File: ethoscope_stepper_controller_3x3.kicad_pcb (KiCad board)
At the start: 2 copper layers, 74.9 x 74.9 mm, 69 parts, among them P1 PWR_JACK_2.1x5.5_SMD_VERT, T1 TERM_BLK, T2 TERM_BLK, T3 TERM_BLK, T4 TERM_BLK, T5 TERM_BLK, T6 TERM_BLK, T7 TERM_BLK, U1 TMC429, U10 DRV8846, U11 TMC429, U12 BUFFER_TRI_STATE, U13 DRV8846, U2 BUFFER_TRI_STATE, U3 DRV8846, U4 DRV8846, U5 DRV8846, U6 TMC429, U7 BUFFER_TRI_STATE, U8 DRV8846, U9 DRV8846

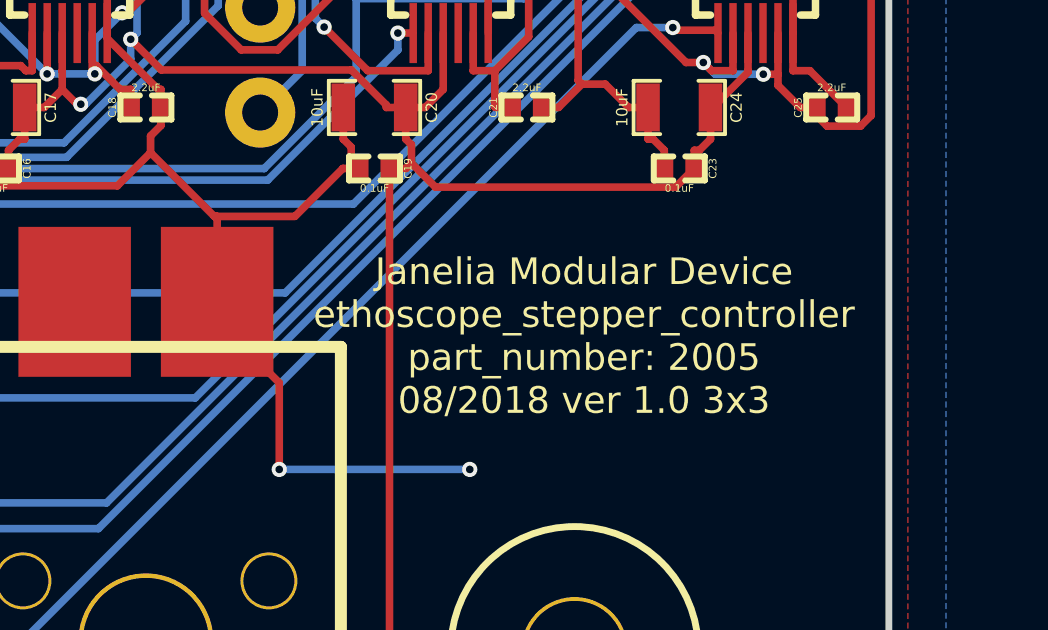
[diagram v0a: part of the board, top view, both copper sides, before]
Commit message: ethoscope_stepper_controller -> ethoscope_stepper_controller_3x3.
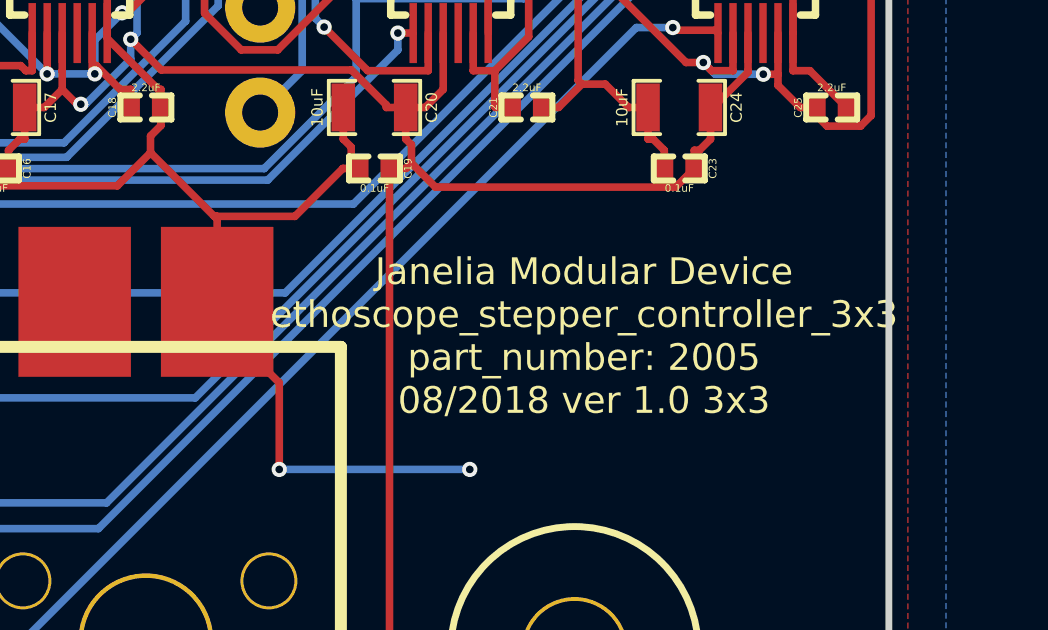
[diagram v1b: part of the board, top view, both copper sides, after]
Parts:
- C1, C11, C12, C13, C15, C16, C18, C19, C2, C21, C22, C23, C25, C3, C5, C6, C8, C9, R1, R10, R11, R12, R13, R14, R15, R16, R17, R2, R3, R4, R5, R6, R7, R8, R9: footprint ethoscope_stepper_controller:SM0402 -> ethoscope_stepper_controller_3x3:SM0402
- C10, C14, C17, C20, C24, C4, C7: footprint ethoscope_stepper_controller:SM0805 -> ethoscope_stepper_controller_3x3:SM0805
- CLK1: footprint ethoscope_stepper_controller:CTS_SMD_4_7X5MM -> ethoscope_stepper_controller_3x3:CTS_SMD_4_7X5MM
- MH1, MH2, MH3, MH4: footprint ethoscope_stepper_controller:MOUNTING_HOLE_4-40 -> ethoscope_stepper_controller_3x3:MOUNTING_HOLE_4-40
- P1: footprint ethoscope_stepper_controller:DCJACK_3PIN_SMD_VERT -> ethoscope_stepper_controller_3x3:DCJACK_3PIN_SMD_VERT
- T1, T2, T3, T4, T5, T6, T7: footprint ethoscope_stepper_controller:TERM_BLK_HDR_4POS_VERT_0.138IN -> ethoscope_stepper_controller_3x3:TERM_BLK_HDR_4POS_VERT_0.138IN
- TEENSY1: footprint ethoscope_stepper_controller:TEENSY_3.5_MIN -> ethoscope_stepper_controller_3x3:TEENSY_3.5_MIN
- U1, U11, U6: footprint ethoscope_stepper_controller:QFN-5x5-32 -> ethoscope_stepper_controller_3x3:QFN-5x5-32
- U10, U13, U3, U4, U5, U8, U9: footprint ethoscope_stepper_controller:VQFN-4x4-24 -> ethoscope_stepper_controller_3x3:VQFN-4x4-24
- U12, U2, U7: footprint ethoscope_stepper_controller:SOT-23-5 -> ethoscope_stepper_controller_3x3:SOT-23-5
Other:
- board text added: "Janelia Modular Device ethoscope_stepper_controller_3x3 part_number: 2005 08/2018 ver 1.0 3x3"
- board text removed: "Janelia Modular Device ethoscope_stepper_controller part_number: 2005 08/2018 ver 1.0 3x3"

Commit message: Finished version 1.0.
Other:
- board text added: "Janelia Modular Device ethoscope_stepper_controller part_number: 2005 08/2018 ver 1.0 3x3"
- board text removed: "Janelia Modular Device ethoscope_stepper_controller_3x3 part_number: 2005 08/2018 ver 1.0 3x3"
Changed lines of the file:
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@@
     (effects (font (size 1.016 1.016) (thickness 0.1905)))
   )
-  (gr_text "Janelia Modular Device\nethoscope_stepper_controller_3x3\npart_number: 2005\n08/2018 ver 1.0 3x3" (at 179.705 118.11) (layer F.SilkS)
+  (gr_text "Janelia Modular Device\nethoscope_stepper_controller\npart_number: 2005\n08/2018 ver 1.0 3x3" (at 179.705 118.11) (layer F.SilkS)
     (effects (font (size 0.889 0.889) (thickness 0.22225)))
   )

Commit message: Rearranged schematics.
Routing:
- net GND: track 490.5 -> 0.00 mm, vias 12 -> 0
- net VAA: track 145.8 -> 0.00 mm, vias 6 -> 0
- net +3V3: track 145.4 -> 0.00 mm, vias 4 -> 0
- net /ENABLE_ALL: track 140.4 -> 0.00 mm, vias 7 -> 0
- net /CS_429_2: track 81.4 -> 0.00 mm
- net /tmc429_0/DIR_1: track 73.2 -> 0.00 mm
- net /tmc429_2/DIR_0: track 70.9 -> 0.00 mm, vias 2 -> 0
- net /tmc429_1/STEP_0: track 67.9 -> 0.00 mm, vias 2 -> 0
- net /tmc429_2/STEP_0: track 66.7 -> 0.00 mm, vias 2 -> 0
- net /MOSI: track 64.5 -> 0.00 mm, vias 3 -> 0
- net /CS_429_1: track 64.2 -> 0.00 mm, vias 1 -> 0
- net /tmc429_0/STEP_1: track 64.0 -> 0.00 mm, vias 2 -> 0
- net /tmc429_1/DIR_0: track 63.9 -> 0.00 mm, vias 2 -> 0
- net /tmc429_1/STEP_2: track 59.1 -> 0.00 mm
- net /tmc429_1/DIR_2: track 54.2 -> 0.00 mm, vias 2 -> 0
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- removed copper zone on B.Cu, net GND
- removed copper zone on F.Cu, net GND
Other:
- outline, holes or cut-outs redrawn
- board text added: "Janelia Modular Device ethoscope_stepper_controller part_number: 2005 09/2018 ver 1.1 3x3"
- board text removed: "Janelia Modular Device ethoscope_stepper_controller part_number: 2005 08/2018 ver 1.0 3x3"

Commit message: Ready for autorouting.
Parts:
- T1, T2, T3, T4, T5, T6, T7: value TERM_BLK -> TERM_BLK_HDR_4POS_VERT_0.138IN
- TEENSY1: value TEENSY_3.5 -> TEENSY_3.5_MIN
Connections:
- net /CLK renamed /ethoscope_3x3/CLK
- net /CS_429_0 renamed /~CS_429_0
- net /CS_429_1 renamed /~CS_429_1
- net /CS_429_2 renamed /~CS_429_2
- net /tmc429_0/DIR_0 renamed /ethoscope_3x3/tmc429_0/DIR_0
- net /tmc429_0/DIR_1 renamed /ethoscope_3x3/tmc429_0/DIR_1
- net /tmc429_0/DIR_2 renamed /ethoscope_3x3/tmc429_0/DIR_2
- net /tmc429_0/MISO_UB renamed /ethoscope_3x3/tmc429_0/MISO_UB
- net /tmc429_0/STEP_0 renamed /ethoscope_3x3/tmc429_0/STEP_0
- net /tmc429_0/STEP_1 renamed /ethoscope_3x3/tmc429_0/STEP_1
- net /tmc429_0/STEP_2 renamed /ethoscope_3x3/tmc429_0/STEP_2
- net /tmc429_0/stepper_driver_0/AISEN renamed /ethoscope_3x3/tmc429_0/stepper_driver_0/AISEN
- net /tmc429_0/stepper_driver_0/A_+ renamed /ethoscope_3x3/tmc429_0/stepper_driver_0/A_+
- net /tmc429_0/stepper_driver_0/A_- renamed /ethoscope_3x3/tmc429_0/stepper_driver_0/A_-
- net /tmc429_0/stepper_driver_0/BISEN renamed /ethoscope_3x3/tmc429_0/stepper_driver_0/BISEN
- net /tmc429_0/stepper_driver_0/B_+ renamed /ethoscope_3x3/tmc429_0/stepper_driver_0/B_+
- net /tmc429_0/stepper_driver_0/B_- renamed /ethoscope_3x3/tmc429_0/stepper_driver_0/B_-
- net /tmc429_0/stepper_driver_1/AISEN renamed /ethoscope_3x3/tmc429_0/stepper_driver_1/AISEN
- net /tmc429_0/stepper_driver_1/A_+ renamed /ethoscope_3x3/tmc429_0/stepper_driver_1/A_+
- net /tmc429_0/stepper_driver_1/A_- renamed /ethoscope_3x3/tmc429_0/stepper_driver_1/A_-
- net /tmc429_0/stepper_driver_1/BISEN renamed /ethoscope_3x3/tmc429_0/stepper_driver_1/BISEN
- net /tmc429_0/stepper_driver_1/B_+ renamed /ethoscope_3x3/tmc429_0/stepper_driver_1/B_+
- net /tmc429_0/stepper_driver_1/B_- renamed /ethoscope_3x3/tmc429_0/stepper_driver_1/B_-
- net /tmc429_0/stepper_driver_2/AISEN renamed /ethoscope_3x3/tmc429_0/stepper_driver_2/AISEN
- net /tmc429_0/stepper_driver_2/A_+ renamed /ethoscope_3x3/tmc429_0/stepper_driver_2/A_+
- net /tmc429_0/stepper_driver_2/A_- renamed /ethoscope_3x3/tmc429_0/stepper_driver_2/A_-
- net /tmc429_0/stepper_driver_2/BISEN renamed /ethoscope_3x3/tmc429_0/stepper_driver_2/BISEN
- net /tmc429_0/stepper_driver_2/B_+ renamed /ethoscope_3x3/tmc429_0/stepper_driver_2/B_+
- net /tmc429_0/stepper_driver_2/B_- renamed /ethoscope_3x3/tmc429_0/stepper_driver_2/B_-
- net /tmc429_1/DIR_0 renamed /ethoscope_3x3/tmc429_1/DIR_0
- net /tmc429_1/DIR_1 renamed /ethoscope_3x3/tmc429_1/DIR_1
- net /tmc429_1/DIR_2 renamed /ethoscope_3x3/tmc429_1/DIR_2
- net /tmc429_1/MISO_UB renamed /ethoscope_3x3/tmc429_1/MISO_UB
- net /tmc429_1/STEP_0 renamed /ethoscope_3x3/tmc429_1/STEP_0
- net /tmc429_1/STEP_1 renamed /ethoscope_3x3/tmc429_1/STEP_1
- net /tmc429_1/STEP_2 renamed /ethoscope_3x3/tmc429_1/STEP_2
- net /tmc429_1/stepper_driver_0/AISEN renamed /ethoscope_3x3/tmc429_1/stepper_driver_0/AISEN
- net /tmc429_1/stepper_driver_0/A_+ renamed /ethoscope_3x3/tmc429_1/stepper_driver_0/A_+
- net /tmc429_1/stepper_driver_0/A_- renamed /ethoscope_3x3/tmc429_1/stepper_driver_0/A_-
- net /tmc429_1/stepper_driver_0/BISEN renamed /ethoscope_3x3/tmc429_1/stepper_driver_0/BISEN
- net /tmc429_1/stepper_driver_0/B_+ renamed /ethoscope_3x3/tmc429_1/stepper_driver_0/B_+
- net /tmc429_1/stepper_driver_0/B_- renamed /ethoscope_3x3/tmc429_1/stepper_driver_0/B_-
- net /tmc429_1/stepper_driver_1/AISEN renamed /ethoscope_3x3/tmc429_1/stepper_driver_1/AISEN
- net /tmc429_1/stepper_driver_1/A_+ renamed /ethoscope_3x3/tmc429_1/stepper_driver_1/A_+
- net /tmc429_1/stepper_driver_1/A_- renamed /ethoscope_3x3/tmc429_1/stepper_driver_1/A_-
- net /tmc429_1/stepper_driver_1/BISEN renamed /ethoscope_3x3/tmc429_1/stepper_driver_1/BISEN
- net /tmc429_1/stepper_driver_1/B_+ renamed /ethoscope_3x3/tmc429_1/stepper_driver_1/B_+
- net /tmc429_1/stepper_driver_1/B_- renamed /ethoscope_3x3/tmc429_1/stepper_driver_1/B_-
- net /tmc429_1/stepper_driver_2/AISEN renamed /ethoscope_3x3/tmc429_1/stepper_driver_2/AISEN
- net /tmc429_1/stepper_driver_2/A_+ renamed /ethoscope_3x3/tmc429_1/stepper_driver_2/A_+
- net /tmc429_1/stepper_driver_2/A_- renamed /ethoscope_3x3/tmc429_1/stepper_driver_2/A_-
- net /tmc429_1/stepper_driver_2/BISEN renamed /ethoscope_3x3/tmc429_1/stepper_driver_2/BISEN
- net /tmc429_1/stepper_driver_2/B_+ renamed /ethoscope_3x3/tmc429_1/stepper_driver_2/B_+
- net /tmc429_1/stepper_driver_2/B_- renamed /ethoscope_3x3/tmc429_1/stepper_driver_2/B_-
- net /tmc429_2/DIR_0 renamed /ethoscope_3x3/tmc_429_2/DIR_0
- net /tmc429_2/MISO_UB renamed /ethoscope_3x3/tmc_429_2/MISO_UB
- net /tmc429_2/STEP_0 renamed /ethoscope_3x3/tmc_429_2/STEP_0
- net /tmc429_2/stepper_driver_0/AISEN renamed /ethoscope_3x3/tmc_429_2/stepper_driver_0/AISEN
- net /tmc429_2/stepper_driver_0/A_+ renamed /ethoscope_3x3/tmc_429_2/stepper_driver_0/A_+
- net /tmc429_2/stepper_driver_0/A_- renamed /ethoscope_3x3/tmc_429_2/stepper_driver_0/A_-
- net /tmc429_2/stepper_driver_0/BISEN renamed /ethoscope_3x3/tmc_429_2/stepper_driver_0/BISEN
- net /tmc429_2/stepper_driver_0/B_+ renamed /ethoscope_3x3/tmc_429_2/stepper_driver_0/B_+
- net /tmc429_2/stepper_driver_0/B_- renamed /ethoscope_3x3/tmc_429_2/stepper_driver_0/B_-
- C11 pad 1: /tmc429_0/stepper_driver_2/VINT -> /ethoscope_3x3/tmc429_0/stepper_driver_2/VINT
- C15 pad 1: /tmc429_1/stepper_driver_0/VINT -> /ethoscope_3x3/tmc429_1/stepper_driver_0/VINT
- C18 pad 1: /tmc429_1/stepper_driver_1/VINT -> /ethoscope_3x3/tmc429_1/stepper_driver_1/VINT
- C21 pad 1: /tmc429_1/stepper_driver_2/VINT -> /ethoscope_3x3/tmc429_1/stepper_driver_2/VINT
- C25 pad 1: /tmc429_2/stepper_driver_0/VINT -> /ethoscope_3x3/tmc_429_2/stepper_driver_0/VINT
- C5 pad 1: /tmc429_0/stepper_driver_0/VINT -> /ethoscope_3x3/tmc429_0/stepper_driver_0/VINT
- C8 pad 1: /tmc429_0/stepper_driver_1/VINT -> /ethoscope_3x3/tmc429_0/stepper_driver_1/VINT
- TEENSY1 pad 22: /ENABLE_ALL -> /~SLEEP
- U10 pad 11: /ENABLE_ALL -> (no net)
- U10 pad 14: /tmc429_1/stepper_driver_2/VINT -> /ethoscope_3x3/tmc429_1/stepper_driver_2/VINT
- U10 pad 17: /tmc429_1/stepper_driver_2/VINT -> /ethoscope_3x3/tmc429_1/stepper_driver_2/VINT
- U10 pad 19: /tmc429_1/stepper_driver_2/VINT -> +3V3
- U10 pad 22: /tmc429_1/stepper_driver_2/VINT -> +3V3
- U10 pad 23: /tmc429_1/stepper_driver_2/VINT -> /~SLEEP
- U10 pad 24: /tmc429_1/stepper_driver_2/VINT -> +3V3
- U10 pad 9: /tmc429_1/stepper_driver_2/VINT -> +3V3
- U13 pad 11: /ENABLE_ALL -> (no net)
- U13 pad 14: /tmc429_2/stepper_driver_0/VINT -> /ethoscope_3x3/tmc_429_2/stepper_driver_0/VINT
- U13 pad 17: /tmc429_2/stepper_driver_0/VINT -> /ethoscope_3x3/tmc_429_2/stepper_driver_0/VINT
- U13 pad 19: /tmc429_2/stepper_driver_0/VINT -> +3V3
- U13 pad 22: /tmc429_2/stepper_driver_0/VINT -> +3V3
- U13 pad 23: /tmc429_2/stepper_driver_0/VINT -> /~SLEEP
- U13 pad 24: /tmc429_2/stepper_driver_0/VINT -> +3V3
- U13 pad 9: /tmc429_2/stepper_driver_0/VINT -> +3V3
- U3 pad 11: /ENABLE_ALL -> (no net)
- U3 pad 14: /tmc429_0/stepper_driver_0/VINT -> /ethoscope_3x3/tmc429_0/stepper_driver_0/VINT
- U3 pad 17: /tmc429_0/stepper_driver_0/VINT -> /ethoscope_3x3/tmc429_0/stepper_driver_0/VINT
- U3 pad 19: /tmc429_0/stepper_driver_0/VINT -> +3V3
- U3 pad 22: /tmc429_0/stepper_driver_0/VINT -> +3V3
- U3 pad 23: /tmc429_0/stepper_driver_0/VINT -> /~SLEEP
- U3 pad 24: /tmc429_0/stepper_driver_0/VINT -> +3V3
- U3 pad 9: /tmc429_0/stepper_driver_0/VINT -> +3V3
- U4 pad 11: /ENABLE_ALL -> (no net)
- U4 pad 14: /tmc429_0/stepper_driver_1/VINT -> /ethoscope_3x3/tmc429_0/stepper_driver_1/VINT
- U4 pad 17: /tmc429_0/stepper_driver_1/VINT -> /ethoscope_3x3/tmc429_0/stepper_driver_1/VINT
- U4 pad 19: /tmc429_0/stepper_driver_1/VINT -> +3V3
- U4 pad 22: /tmc429_0/stepper_driver_1/VINT -> +3V3
- U4 pad 23: /tmc429_0/stepper_driver_1/VINT -> /~SLEEP
- U4 pad 24: /tmc429_0/stepper_driver_1/VINT -> +3V3
- U4 pad 9: /tmc429_0/stepper_driver_1/VINT -> +3V3
- U5 pad 11: /ENABLE_ALL -> (no net)
- U5 pad 14: /tmc429_0/stepper_driver_2/VINT -> /ethoscope_3x3/tmc429_0/stepper_driver_2/VINT
- U5 pad 17: /tmc429_0/stepper_driver_2/VINT -> /ethoscope_3x3/tmc429_0/stepper_driver_2/VINT
- U5 pad 19: /tmc429_0/stepper_driver_2/VINT -> +3V3
- U5 pad 22: /tmc429_0/stepper_driver_2/VINT -> +3V3
- U5 pad 23: /tmc429_0/stepper_driver_2/VINT -> /~SLEEP
- U5 pad 24: /tmc429_0/stepper_driver_2/VINT -> +3V3
- U5 pad 9: /tmc429_0/stepper_driver_2/VINT -> +3V3
- U8 pad 11: /ENABLE_ALL -> (no net)
- U8 pad 14: /tmc429_1/stepper_driver_0/VINT -> /ethoscope_3x3/tmc429_1/stepper_driver_0/VINT
- U8 pad 17: /tmc429_1/stepper_driver_0/VINT -> /ethoscope_3x3/tmc429_1/stepper_driver_0/VINT
- U8 pad 19: /tmc429_1/stepper_driver_0/VINT -> +3V3
- U8 pad 22: /tmc429_1/stepper_driver_0/VINT -> +3V3
- U8 pad 23: /tmc429_1/stepper_driver_0/VINT -> /~SLEEP
- U8 pad 24: /tmc429_1/stepper_driver_0/VINT -> +3V3
- U8 pad 9: /tmc429_1/stepper_driver_0/VINT -> +3V3
- U9 pad 11: /ENABLE_ALL -> (no net)
- U9 pad 14: /tmc429_1/stepper_driver_1/VINT -> /ethoscope_3x3/tmc429_1/stepper_driver_1/VINT
- U9 pad 17: /tmc429_1/stepper_driver_1/VINT -> /ethoscope_3x3/tmc429_1/stepper_driver_1/VINT
- U9 pad 19: /tmc429_1/stepper_driver_1/VINT -> +3V3
- U9 pad 22: /tmc429_1/stepper_driver_1/VINT -> +3V3
- U9 pad 23: /tmc429_1/stepper_driver_1/VINT -> /~SLEEP
- U9 pad 24: /tmc429_1/stepper_driver_1/VINT -> +3V3
- U9 pad 9: /tmc429_1/stepper_driver_1/VINT -> +3V3
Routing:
- net GND: track 0.00 -> 6.50 mm
- net +3V3: track 0.00 -> 5.70 mm
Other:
- net class SIGNAL: trace_width 0.254 -> 0.2032

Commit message: Finished autorouting.
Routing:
- net GND: track 6.50 -> 441.3 mm, vias 0 -> 4
- net +3V3: track 5.70 -> 415.5 mm, vias 0 -> 15
- net /~SLEEP: track 0.00 -> 150.4 mm, vias 0 -> 7
- net VAA: track 0.00 -> 140.2 mm, vias 0 -> 8
- net /ethoscope_3x3/tmc_429_2/STEP_0: track 0.00 -> 74.3 mm, vias 0 -> 2
- net /MOSI: track 0.00 -> 73.8 mm, vias 0 -> 3
- net /~CS_429_2: track 0.00 -> 69.1 mm, vias 0 -> 3
- net /ethoscope_3x3/tmc429_0/DIR_1: track 0.00 -> 68.7 mm, vias 0 -> 2
- net /ethoscope_3x3/tmc_429_2/DIR_0: track 0.00 -> 67.1 mm, vias 0 -> 2
- net /ethoscope_3x3/tmc429_0/STEP_1: track 0.00 -> 64.3 mm, vias 0 -> 2
- net /~CS_429_1: track 0.00 -> 63.9 mm, vias 0 -> 1
- net /ethoscope_3x3/tmc429_1/STEP_2: track 0.00 -> 61.9 mm
- net /ethoscope_3x3/tmc429_1/STEP_0: track 0.00 -> 61.9 mm, vias 0 -> 2
- net /ethoscope_3x3/tmc429_1/DIR_2: track 0.00 -> 58.5 mm, vias 0 -> 2
- net /ethoscope_3x3/tmc429_1/DIR_0: track 0.00 -> 57.7 mm, vias 0 -> 2
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
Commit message: Finished version 1.0.
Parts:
- added L1: LED_24V_RED, ethoscope_stepper_controller_3x3:LED_555-3XXX_R, F.Cu at (153.7, 134.0)
- added L2: LED_5V_GRN, ethoscope_stepper_controller_3x3:LED_555-3XXX_G, F.Cu at (151.1, 134.0)
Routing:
- net +3V3: track 415.5 -> 460.5 mm
- net GND: track 441.3 -> 455.9 mm
- net VAA: track 140.2 -> 152.0 mm
- net /ethoscope_3x3/tmc_429_2/stepper_driver_0/A_+: track 39.6 -> 40.2 mm
- added copper zone on B.Cu, net GND
- added copper zone on F.Cu, net VAA
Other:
- rule solder_mask_min_width: 0.25 -> 0.1016
- board text added: "0"
- board text added: "1"
- board text added: "2"
- board text added: "3"
- board text added: "4"
- board text added: "5"
- board text added: "6"
- board text added: "POWER"
- board text added: "USB"

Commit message: Progress towards v1.2
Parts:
- R10, R11, R12, R13, R14, R16, R17, R2, R3, R4, R5, R6, R7, R9: value 5.1 -> 2.2; footprint ethoscope_stepper_controller_3x3:SM0402 -> footprints:SM0402
- TEENSY1: value TEENSY_3.5_MIN -> TEENSY_3.5
- moved C17 4.49 mm to (164.5, 111.1), turned to 0 degrees
- moved C20 4.49 mm to (177.2, 111.1), turned to 0 degrees
- moved C24 4.49 mm to (187.3, 111.1), turned to 0 degrees
- moved C4 4.49 mm to (164.5, 78.1), turned to 0 degrees
- moved C10 4.49 mm to (164.5, 94.6), turned to 0 degrees
- moved C14 4.49 mm to (177.2, 94.6), turned to 0 degrees
- moved C7 4.49 mm to (187.3, 94.6), turned to 0 degrees
- moved C13 4.45 mm to (177.2, 96.3), turned to 0 degrees
- moved C3 4.45 mm to (164.5, 79.8), turned to 0 degrees
- moved C6 4.45 mm to (187.3, 96.3), turned to 0 degrees
- moved C9 4.45 mm to (164.5, 96.3), turned to 0 degrees
- moved C16 4.45 mm to (164.5, 112.8), turned to 0 degrees
- moved C19 4.45 mm to (177.2, 112.8), turned to 0 degrees
- moved C23 4.45 mm to (187.3, 112.8), turned to 0 degrees
- moved C15 1.20 mm to (177.2, 93.0)
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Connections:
- U10 pad 8: (no net) -> +3V3
- U10 pad 9: +3V3 -> (no net)
- U13 pad 8: (no net) -> +3V3
- U13 pad 9: +3V3 -> (no net)
- U3 pad 8: (no net) -> +3V3
- U3 pad 9: +3V3 -> (no net)
- U4 pad 8: (no net) -> +3V3
- U4 pad 9: +3V3 -> (no net)
- U5 pad 8: (no net) -> +3V3
- U5 pad 9: +3V3 -> (no net)
- U8 pad 8: (no net) -> +3V3
- U8 pad 9: +3V3 -> (no net)
- U9 pad 8: (no net) -> +3V3
- U9 pad 9: +3V3 -> (no net)
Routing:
- net /ethoscope_3x3/tmc429_0/stepper_driver_1/BISEN: track 55.4 -> 5.58 mm
- net /~SLEEP: track 150.4 -> 125.2 mm, vias 7 -> 8
- net /MOSI: track 73.8 -> 50.3 mm
- net VAA: track 152.0 -> 172.0 mm, vias 8 -> 9
- net GND: track 455.9 -> 439.6 mm, vias 4 -> 0
- net /ethoscope_3x3/tmc429_1/stepper_driver_0/BISEN: track 2.83 -> 18.6 mm
- net /ethoscope_3x3/tmc429_1/stepper_driver_1/BISEN: track 2.83 -> 18.3 mm
- net /ethoscope_3x3/tmc429_0/stepper_driver_2/BISEN: track 2.83 -> 18.1 mm
- net /ethoscope_3x3/tmc429_0/stepper_driver_0/VINT: track 19.3 -> 5.16 mm
- net +3V3: track 460.5 -> 453.1 mm, vias 15 -> 14
- net /ethoscope_3x3/tmc429_1/STEP_2: track 61.9 -> 55.0 mm, vias 0 -> 2
- net /ethoscope_3x3/tmc429_1/DIR_0: track 57.7 -> 64.0 mm
- net /ethoscope_3x3/tmc_429_2/STEP_0: track 74.3 -> 68.0 mm
- net /ethoscope_3x3/tmc429_1/STEP_0: track 61.9 -> 67.7 mm
- net /ethoscope_3x3/tmc429_0/STEP_0: track 52.2 -> 47.5 mm
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- added copper zone on F.Cu, net GND
- added copper zone on B.Cu, net VAA
- removed copper zone on B.Cu, net GND
- removed copper zone on F.Cu, net VAA
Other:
- net class SIGNAL: via_dia 0.508 -> 0.4064; via_drill 0.254 -> 0.2032
- rule pad_to_mask_clearance: 0 -> 0.001
- rule solder_mask_min_width: 0.1016 -> 0.1
- rule via_min_drill: 0.254 -> 0.2032
- rule via_min_size: 0.508 -> 0.4064
- board text added: "Janelia Modular Device ethoscope_stepper_controller part_number: 2005 02/2019 ver 1.2 3x3"
- board text removed: "Janelia Modular Device ethoscope_stepper_controller part_number: 2005 09/2018 ver 1.1 3x3"
